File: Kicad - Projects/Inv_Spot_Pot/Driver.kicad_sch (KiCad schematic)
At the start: 3 parts

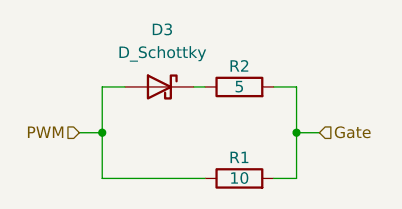
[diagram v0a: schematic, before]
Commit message: Updated PCB
Fixed some footprints, increased insulation and improved board segmentation - segmentation still needs some work
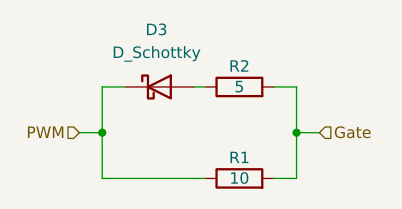
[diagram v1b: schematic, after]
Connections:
- net PWM: now also D3.1 (K); no longer D3.2 (A)
- net at R2.1: now also D3.2 (A); no longer D3.1 (K)
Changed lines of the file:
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@@
 		(lib_id "Device:D_Schottky")
 		(at 83.82 71.12 0)
-		(mirror y)
 		(unit 1)
 		(exclude_from_sim no)
@@
 		(on_board yes)
 		(dnp no)
-		(fields_autoplaced yes)
 		(property "Reference" "D3"
-			(at 84.1375 64.77 0)
+			(at 83.5025 64.77 0)
 			(effects
 				(font
@@
 		)
 		(property "Value" "D_Schottky"
-			(at 84.1375 67.31 0)
+			(at 83.5025 67.31 0)
 			(effects
 				(font
